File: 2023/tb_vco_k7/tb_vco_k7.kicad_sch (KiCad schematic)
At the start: 12 parts, among them M1 PMOS_OR1, M10 NMOS_OR1, M13 PMOS_OR1, M14 NMOS_OR1, M17 PMOS_OR1, M18 NMOS_OR1, M2 NMOS_OR1, M21 PMOS_OR1, M22 NMOS_OR1, M9 PMOS_OR1

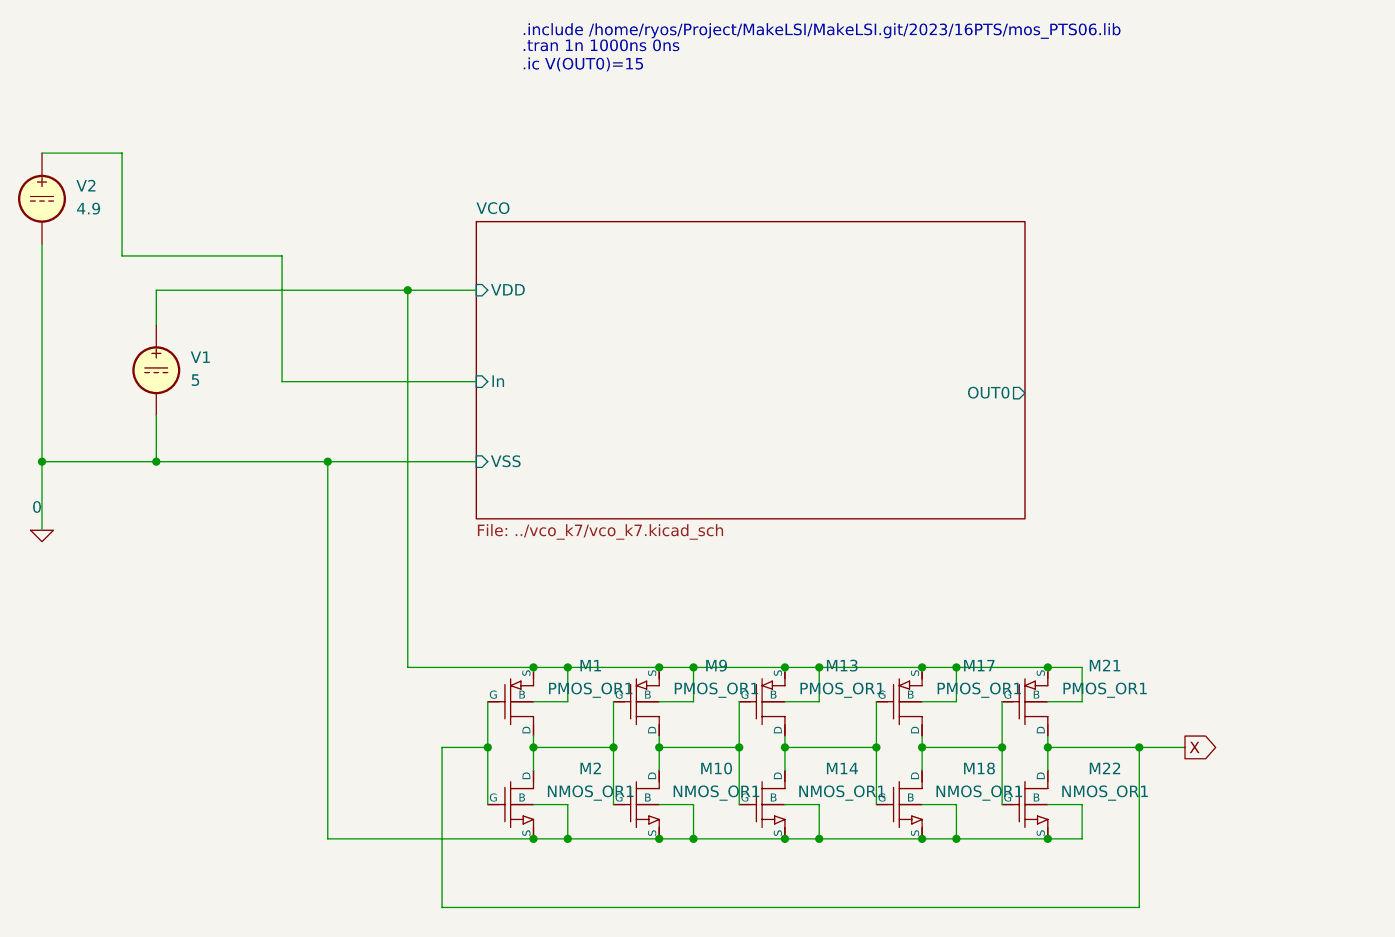
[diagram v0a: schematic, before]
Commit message: VCO 回路図を見直してちゃんとシミュレーションできるようにした。
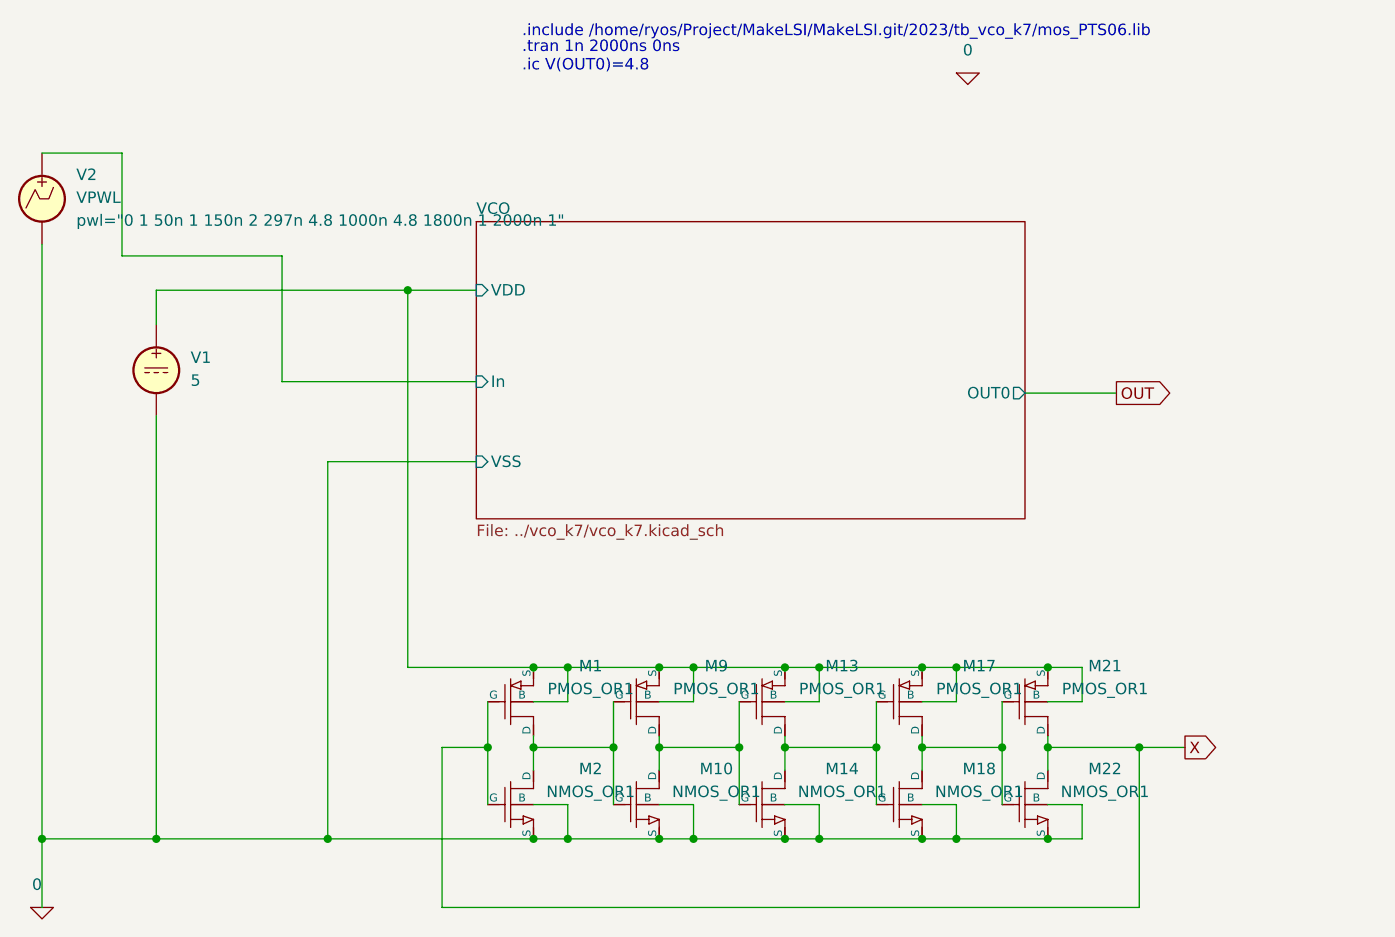
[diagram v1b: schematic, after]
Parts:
- removed V2: 4.9, symbol Simulation_SPICE:VDC
- added V2: VPWL, symbol Simulation_SPICE:VPWL
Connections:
- net 0: now also V2.2
- net VCO/In: now also V2.1
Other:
- note added: ".include /home/ryos/Project/MakeLSI/MakeLSI.git/2023/tb_vco_k7/mos_PTS06.lib"
- note added: ".tran 1n 2000ns 0ns .ic V(OUT0)=4.8"
- note removed: ".include /home/ryos/Project/MakeLSI/MakeLSI.git/2023/16PTS/mos_PTS06.lib"
- note removed: ".tran 1n 1000ns 0ns .ic V(OUT0)=15"
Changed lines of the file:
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@@
   (junction (at 193.04 135.89) (diameter 0) (color 0 0 0 0)
   )
-  (junction (at 81.28 104.14) (diameter 0) (color 0 0 0 0)
+  (junction (at 113.03 146.05) (diameter 0) (color 0 0 0 0)
+  )
+  (junction (at 81.28 146.05) (diameter 0) (color 0 0 0 0)
   )
   (junction (at 149.86 127) (diameter 0) (color 0 0 0 0)
@@
   (junction (at 179.07 127) (diameter 0) (color 0 0 0 0)
   )
-  (junction (at 113.03 104.14) (diameter 0) (color 0 0 0 0)
-  )
   (junction (at 121.92 85.09) (diameter 0) (color 0 0 0 0)
   )
@@
   (junction (at 179.07 146.05) (diameter 0) (color 0 0 0 0)
   )
-  (junction (at 93.98 104.14) (diameter 0) (color 0 0 0 0)
+  (junction (at 93.98 146.05) (diameter 0) (color 0 0 0 0)
   )
   (junction (at 163.83 127) (diameter 0) (color 0 0 0 0)
@@
     (stroke (width 0) (type default))
   )
-  (wire (pts (xy 93.98 104.14) (xy 113.03 104.14))
+  (wire (pts (xy 93.98 146.05) (xy 113.03 146.05))
     (stroke (width 0) (type default))
   )
@@
     (stroke (width 0) (type default))
   )
-  (wire (pts (xy 81.28 80.01) (xy 81.28 104.14))
+  (wire (pts (xy 81.28 80.01) (xy 81.28 146.05))
     (stroke (width 0) (type default))
   )
@@
     (stroke (width 0) (type default))
   )
-  (wire (pts (xy 81.28 104.14) (xy 81.28 111.76))
-    (stroke (width 0) (type default))
-  )
-  (wire (pts (xy 93.98 99.06) (xy 93.98 104.14))
+  (wire (pts (xy 81.28 146.05) (xy 81.28 153.67))
+    (stroke (width 0) (type default))
+  )
+  (wire (pts (xy 93.98 99.06) (xy 93.98 146.05))
     (stroke (width 0) (type default))
   )
@@
     (stroke (width 0) (type default))
   )
+  (wire (pts (xy 190.5 96.52) (xy 200.66 96.52))
+    (stroke (width 0) (type default))
+  )
   (wire (pts (xy 179.07 142.24) (xy 182.88 142.24))
     (stroke (width 0) (type default))
@@
     (stroke (width 0) (type default))
   )
-  (wire (pts (xy 81.28 104.14) (xy 93.98 104.14))
+  (wire (pts (xy 81.28 146.05) (xy 93.98 146.05))
     (stroke (width 0) (type default))
   )
@@
     (stroke (width 0) (type default))
   )
-  (text ".include /home/ryos/Project/MakeLSI/MakeLSI.git/2023/16PTS/mos_PTS06.lib\n"
+  (text ".include /home/ryos/Project/MakeLSI/MakeLSI.git/2023/tb_vco_k7/mos_PTS06.lib\n"
     (at 134.62 57.15 0)
     (effects (font (size 1.27 1.27)) (justify left bottom))
   )
-  (text ".tran 1n 1000ns 0ns\n.ic V(OUT0)=15" (at 134.62 60.96 0)
+  (text ".tran 1n 2000ns 0ns\n.ic V(OUT0)=4.8" (at 134.62 60.96 0)
     (effects (font (size 1.27 1.27)) (justify left bottom))
   )
@@
     )
   )
+  (global_label "OUT" (shape output) (at 200.66 96.52 0) (fields_autoplaced)
+    (effects (font (size 1.27 1.27)) (justify left))
+    (property "Intersheetrefs" "${INTERSHEET_REFS}" (at 207.2738 96.52 0)
+      (effects (font (size 1.27 1.27)) (justify left) hide)
+    )
+  )
   (symbol (lib_id "OR1Symbols:PMOS_OR1") (at 173.99 130.81 0) (unit 1)
     (in_bom yes) (on_board yes) (dnp no) (fields_autoplaced)
@@
     )
   )
-  (symbol (lib_id "OR1Symbols:0") (at 81.28 111.76 0) (unit 1)
-    (in_bom yes) (on_board yes) (dnp no) (fields_autoplaced)
-    (property "Reference" "#GND01" (at 81.28 114.3 0)
-      (effects (font (size 1.27 1.27)) hide)
-    )
-    (property "Value" "0" (at 81.28 109.22 0)
+  (symbol (lib_id "OR1Symbols:0") (at 81.28 153.67 0) (unit 1)
+    (in_bom yes) (on_board yes) (dnp no) (fields_autoplaced)
+    (property "Reference" "#GND01" (at 81.28 156.21 0)
+      (effects (font (size 1.27 1.27)) hide)
+    )
+    (property "Value" "0" (at 81.28 151.13 0)
       (effects (font (size 1.27 1.27)) (justify right))
     )
-    (property "Footprint" "" (at 85.09 111.76 0)
-      (effects (font (size 1.27 1.27)) hide)
-    )
-    (property "Datasheet" "" (at 85.09 111.76 0)
+    (property "Footprint" "" (at 85.09 153.67 0)
+      (effects (font (size 1.27 1.27)) hide)
+    )
+    (property "Datasheet" "" (at 85.09 153.67 0)
       (effects (font (size 1.27 1.27)) hide)
     )
@@
         (path "/75cba549-0e80-46a3-a310-5c4e6c452e77"
           (reference "#GND01") (unit 1)
-        )
-      )
-    )
-  )
-  (symbol (lib_id "Simulation_SPICE:VDC") (at 81.28 74.93 0) (unit 1)
-    (in_bom yes) (on_board yes) (dnp no) (fields_autoplaced)
-    (property "Reference" "V2" (at 85.09 73.5302 0)
-      (effects (font (size 1.27 1.27)) (justify left))
-    )
-    (property "Value" "4.9" (at 85.09 76.0702 0)
-      (effects (font (size 1.27 1.27)) (justify left))
-    )
-    (property "Footprint" "" (at 81.28 74.93 0)
-      (effects (font (size 1.27 1.27)) hide)
-    )
-    (property "Datasheet" "~" (at 81.28 74.93 0)
-      (effects (font (size 1.27 1.27)) hide)
-    )
-    (property "Sim.Pins" "1=+ 2=-" (at 81.28 74.93 0)
-      (effects (font (size 1.27 1.27)) hide)
-    )
-    (property "Sim.Type" "DC" (at 81.28 74.93 0)
-      (effects (font (size 1.27 1.27)) hide)
-    )
-    (property "Sim.Device" "V" (at 81.28 74.93 0)
-      (effects (font (size 1.27 1.27)) (justify left) hide)
-    )
-    (pin "1")
-    (pin "2")
-    (instances
-      (project "tb_vco_k7"
-        (path "/75cba549-0e80-46a3-a310-5c4e6c452e77"
-          (reference "V2") (unit 1)
         )
       )
@@
         )
       )
+    )
+  )
+  (symbol (lib_id "Simulation_SPICE:VPWL") (at 81.28 74.93 0) (unit 1)
+    (in_bom yes) (on_board yes) (dnp no) (fields_autoplaced)
+    (property "Reference" "V2" (at 85.09 72.2602 0)
+      (effects (font (size 1.27 1.27)) (justify left))
+    )
+    (property "Value" "VPWL" (at 85.09 74.8002 0)
+      (effects (font (size 1.27 1.27)) (justify left))
+    )
+    (property "Footprint" "" (at 81.28 74.93 0)
+      (effects (font (size 1.27 1.27)) hide)
+    )
+    (property "Datasheet" "~" (at 81.28 74.93 0)
+      (effects (font (size 1.27 1.27)) hide)
+    )
+    (property "Sim.Pins" "1=+ 2=-" (at 81.28 74.93 0)
+      (effects (font (size 1.27 1.27)) hide)
+    )
+    (property "Sim.Device" "V" (at 81.28 74.93 0)
+      (effects (font (size 1.27 1.27)) (justify left) hide)
+    )
+    (property "Sim.Params" "pwl=\"0  1 50n 1 150n 2 297n 4.8 1000n 4.8 1800n 1 2000n 1\"" (at 85.09 77.3402 0)
+      (effects (font (size 1.27 1.27)) (justify left))
+    )
+    (property "Sim.Type" "PWL" (at 81.28 74.93 0)
+      (effects (font (size 1.27 1.27)) hide)
+    )
+    (pin "1")
+    (pin "2")
+    (instances
+      (project "tb_vco_k7"
+        (path "/75cba549-0e80-46a3-a310-5c4e6c452e77"
+          (reference "V2") (unit 1)
+        )
+      )
+    )
+  )
+  (symbol (lib_id "Simulation_SPICE:0") (at 184.15 60.96 0) (unit 1)
+    (in_bom yes) (on_board yes) (dnp no) (fields_autoplaced)
+    (property "Reference" "#GND02" (at 184.15 63.5 0)
+      (effects (font (size 1.27 1.27)) hide)
+    )
+    (property "Value" "0" (at 184.15 58.42 0)
+      (effects (font (size 1.27 1.27)))
+    )
+    (property "Footprint" "" (at 184.15 60.96 0)
+      (effects (font (size 1.27 1.27)) hide)
+    )
+    (property "Datasheet" "~" (at 184.15 60.96 0)
+      (effects (font (size 1.27 1.27)) hide)
+    )
+    (pin "1")
+    (instances
+      (project "tb_vco_k7"
+        (path "/75cba549-0e80-46a3-a310-5c4e6c452e77"
+          (reference "#GND02") (unit 1)
+        )
+      )
